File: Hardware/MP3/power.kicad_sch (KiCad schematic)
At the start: 11 parts, among them IC1 MCP73871-2CCI_ML, U1 TPS63002DRCR

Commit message: Large additions, DAC schematic work started
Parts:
- added C21, C23: 10uF, Capacitor_SMD:C_0402_1005Metric, symbol Device:C_Small
- added C22: 4.7uF, Capacitor_SMD:C_0402_1005Metric, symbol Device:C_Small
- added C24: 0.1uF, Capacitor_SMD:C_0402_1005Metric, symbol Device:C_Small
- added C5: 10uF, Capacitor_SMD:C_0603_1608Metric, symbol Device:C_Small
- added R10: 100k, Resistor_SMD:R_0402_1005Metric, symbol Device:R_Small
- added R11, R24, R7, R8: 10k, Resistor_SMD:R_0402_1005Metric, symbol Device:R_Small
- added R2: 2.49k, Resistor_SMD:R_0402_1005Metric, symbol Device:R_Small
- added R23: 56k, Resistor_SMD:R_0402_1005Metric, symbol Device:R_Small
- added R3: 24.9k, Resistor_SMD:R_0402_1005Metric, symbol Device:R_Small
- added R4: 2.0k, Resistor_SMD:R_0402_1005Metric, symbol Device:R_Small
- added R9: 330k, Resistor_SMD:R_0402_1005Metric, symbol Device:R_Small
- added TH1: Thermistor_NTC 10k, symbol Device:Thermistor_NTC
- added TP8: TestPoint, TestPoint:TestPoint_Pad_D1.5mm, symbol Connector:TestPoint
- added U5: SC4215, iclr:SOIC127P599X175-9N, symbol iclr:RT9025-25GSP
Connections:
- net 5V: now also C21.1, C22.1, TP8.1, U5.2 (EN), U5.3 (VIN)
- net GND: now also IC1.3 (SEL), IC1.9 (~{TE}), C21.2, C22.2, C23.1, C24.1, C5.2, R10.2, R2.1, R24.2, R3.1, R4.2, TH1.2, U5.8 (GND), U5.9 (GND)
- net VBUS: now also C5.1, R9.1; no longer IC1.2 (VPCC)
- net at IC1.12 (PROG3): now also R3.2
- net at IC1.13 (PROG1): now also R2.2
- net CE: now reaches IC1.17 (CE)
- net CE: now also R11.2
- net 3V3: now reaches IC1.4 (PROG2)
- net 3V3: now also R11.1, R7.1, R8.2
- net at IC1.5 (THERM): now also TH1.1
- net PG: now reaches IC1.6 (~{PG})
- net PG: now also R7.2
- net STAT2: now reaches IC1.7 (STAT2)
- net STAT2: now also R8.1
- net LBO: now reaches IC1.8 (STAT1/~{LBO})
- net Vout renamed MCPout
- new net: IC1.2 (VPCC), R10.1, R9.2
- new net +A3V3: C23.2, C24.2, R23.1, U5.6 (VOUT)
- new net FBIn: R23.2, R24.1, U5.7 (ADJ)
- no-connect marks 0 -> 2
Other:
- note added: "PROG2 pulled high rather than low, through 2k resistor"
- moved on the sheet: C1, C2, C20, C3, C6, L1, R1, U1

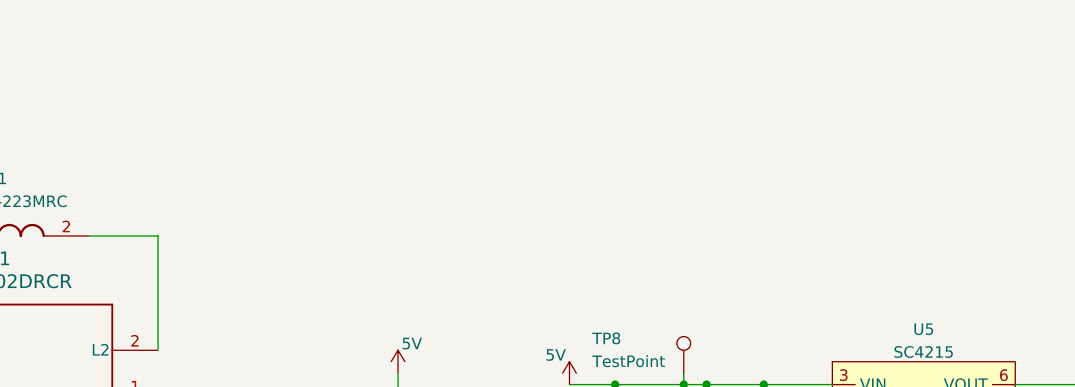
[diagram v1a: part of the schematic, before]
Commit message: feat: Made some changes to the DAC. Explicitly using register control (using I2C) with PCM audio. Planning to use 5.2V buck on 5V line, then Low noise LDO VREF for DAC, another for AMP power, and a 3v3 low noise LDO for DAC too.
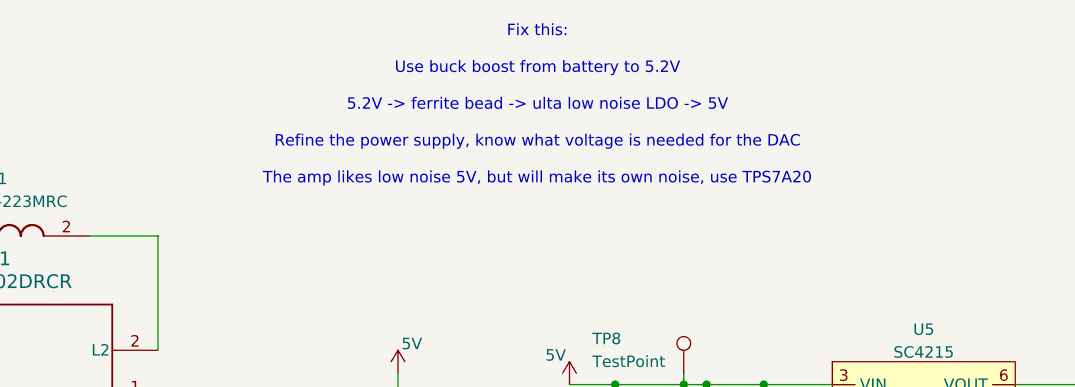
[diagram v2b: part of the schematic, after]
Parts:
- TH1: footprint (none) -> Resistor_SMD:R_0402_1005Metric
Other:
- note added: "Fix this: Use buck boost from battery to 5.2V 5.2V -> ferrite bead -> ulta low noise LDO -> 5V Refine the power supply, know what voltage is needed for the DAC The amp likes low noise 5V, but will make its own noise, use TPS7A20"
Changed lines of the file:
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@@
 	(generator_version "9.0")
 	(paper "A4")
+	(text "Fix this:\n\nUse buck boost from battery to 5.2V\n\n5.2V -> ferrite bead -> ulta low noise LDO -> 5V \n\nRefine the power supply, know what voltage is needed for the DAC\n\nThe amp likes low noise 5V, but will make its own noise, use TPS7A20\n"
+		(exclude_from_sim no)
+		(at 171.704 19.812 0)
+		(effects
+			(font
+				(size 1.27 1.27)
+			)
+		)
+	)
 	(text "MCP73871-1CC\n-2 means charges up to 4.2V\nfirst C means has 6 hour safety timer for charging\nsecond C means 3.1V Low battery threshold"
 		(exclude_from_sim no)
@@
 			)
 		)
-		(property "Footprint" ""
+		(property "Footprint" "Resistor_SMD:R_0402_1005Metric"
 			(at 147.32 140.97 0)
 			(effects

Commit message: feat: Large progress made on the power system. Next steps, find oscillator, sort out LDO footprints, add OLED connectors and encoder connector.
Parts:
- removed C21, C23: 10uF, Capacitor_SMD:C_0402_1005Metric, symbol Device:C_Small
- removed C22: 4.7uF, Capacitor_SMD:C_0402_1005Metric, symbol Device:C_Small
- removed C24: 0.1uF, Capacitor_SMD:C_0402_1005Metric, symbol Device:C_Small
- removed R23: 56k, Resistor_SMD:R_0402_1005Metric, symbol Device:R_Small
- removed R24: 10k, Resistor_SMD:R_0402_1005Metric, symbol Device:R_Small
- removed TP8: TestPoint, TestPoint:TestPoint_Pad_D1.5mm, symbol Connector:TestPoint
- removed U5: SC4215, iclr:SOIC127P599X175-9N, symbol iclr:RT9025-25GSP
- added C31, C32, C33, C34: 1uF, Capacitor_SMD:C_0402_1005Metric, symbol Device:C_Small
- added C35: 1nF, Capacitor_SMD:C_0402_1005Metric, symbol Device:C_Small
- added R15: 1.96MΩ, Resistor_SMD:R_0402_1005Metric, symbol Device:R_Small
- added R16: 208kΩ, Resistor_SMD:R_0603_1608Metric, symbol Device:R_Small
- added U3: TPS7A20xxxDQN, Package_TO_SOT_SMD:SOT-23-5, symbol Regulator_Linear:TPS7A20xxxDQN
- added U4, U6: TPS7A20xxxDQN, Package_SON:Texas_X2SON-4_1x1mm_P0.65mm, symbol Regulator_Linear:TPS7A20xxxDQN
- C2: value 10uF -> 22uF
- C3: value 10uF -> 47uF
- U1: value TPS63002DRCR -> TPS63000DRCR
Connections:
- net +A3V3: now also U6.1 (OUT)
- net GND: now also C31.1, C32.1, C33.1, C34.1, R16.2, U3.2 (GND), U3.5 (Pad)
- net 5V renamed +5.2V
- net +5.2V: now also C31.2, C33.2, C34.2, C35.1, R15.1, U3.3 (EN), U3.4 (IN), U4.4 (IN), U6.4 (IN); no longer U1.10 (FB)
- new net +5V: U4.1 (OUT)
- new net +A5V: C32.2, U3.1 (OUT)
- new net FB: C35.2, R15.2, R16.1, U1.10 (FB)
- no-connect marks 2 -> 0
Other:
- moved on the sheet: C2, C3
